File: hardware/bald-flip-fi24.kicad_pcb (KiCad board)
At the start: 4 copper layers, 67.3 x 37.3 mm, 35 parts, among them J1 Flipper Header, J2 USB4105-GF-A, J3 Flipper Board Outline (Large), Q1 DMN2058U, Q2 DMN2058U, SW1 5V Src, SW2 nRF PWR, SW3 Boot, SW4 Reset, SW5 esp PWR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

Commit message: moved nrf24 to front, I like it better
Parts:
- added D5: nRF, LED_SMD:LED_0805_2012Metric_Pad1.15x1.40mm_HandSolder, F.Cu at (141.2, 105.1)
- added R12: 4k7, Resistor_SMD:R_0805_2012Metric, F.Cu at (137.5, 105.1)
- D1: footprint LED_SMD:LED_1206_3216Metric -> LED_SMD:LED_0805_2012Metric_Pad1.15x1.40mm_HandSolder
- D2: value 3v3 -> ESP; footprint LED_SMD:LED_1206_3216Metric -> LED_SMD:LED_0805_2012Metric_Pad1.15x1.40mm_HandSolder
- TP1: moved to B.Cu
- U2: moved to F.Cu
- moved R2 42.9 mm to (176.8, 101.7)
- moved D2 42.1 mm to (180.7, 101.7)
- moved TP1 28.2 mm to (151.0, 104.0), turned to -90 degrees
- moved D1 27.9 mm to (141.0, 94.4)
- moved R1 24.1 mm to (140.9, 96.7)
- moved C5 19.3 mm to (121.3, 99.5), turned to 180 degrees
- moved C4 15.5 mm to (134.2, 99.5), turned to 0 degrees
- moved C1 14.6 mm to (121.3, 104.7), turned to 180 degrees
- moved U2 12.0 mm to (143.9, 119.8)
- moved U3 10.3 mm to (127.6, 102.1), turned to 180 degrees
- moved J3 9.97 mm to (123.5, 109.2)
- moved C2 1.90 mm to (173.1, 101.7)
- moved R4 1.64 mm to (169.4, 101.7)
- moved C3 1.60 mm to (158.2, 101.7)
- moved R3 1.56 mm to (165.7, 101.7)
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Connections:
- R2 pad 1: +3V3 -> /esp_VCC
- R4 pad 1: +3V3 -> /esp_VCC
- R5 pad 1: +3V3 -> /esp_VCC

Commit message: re-worked SPi signals, need to consider if firmware can handle moving CS. Cleaned up some silk (for now).
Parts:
- added NT1: NetTie_2, NetTie:NetTie-2_SMD_Pad0.5mm, F.Cu at (133.4, 124.7)
- added NT2: NetTie_2, NetTie:NetTie-2_SMD_Pad0.5mm, F.Cu at (135.9, 124.6)
- added NT3: NetTie_2, NetTie:NetTie-2_SMD_Pad0.5mm, F.Cu at (123.2, 124.6)
- added NT4: NetTie_2, NetTie:NetTie-2_SMD_Pad0.5mm, F.Cu at (125.8, 124.6)
- added NT5: NetTie_2, NetTie:NetTie-2_SMD_Pad0.5mm, F.Cu at (128.3, 124.6)
- added NT6: NetTie_2, NetTie:NetTie-2_SMD_Pad0.5mm, F.Cu at (130.8, 124.6)
- J3: moved to B.Cu
- SW1: value 5V Src -> 5V
- SW2: value nRF PWR -> nRF
- SW5: value esp PWR -> esp
- moved D3 24.1 mm to (150.2, 121.8), turned to 180 degrees
- moved D4 21.0 mm to (150.1, 116.2), turned to 180 degrees
- moved R1 1.47 mm to (141.0, 98.2)
- moved D1 1.40 mm to (141.0, 95.8)
- moved R7 0.95 mm to (141.0, 100.5), turned to 180 degrees
- moved R10 0.50 mm to (148.8, 123.7)
- turned J3 to 180 degrees
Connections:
- U1 pad 13: unconnected-(U1-GPIO10/ADC1_CH9-Pad13) -> /CS
- U1 pad 14: unconnected-(U1-GPIO11/ADC2_CH0-Pad14) -> /MOSI
- U1 pad 15: unconnected-(U1-GPIO12/ADC2_CH1-Pad15) -> /SCK
- U1 pad 16: unconnected-(U1-GPIO13/ADC2_CH2-Pad16) -> /MISO
- U2 pad 3: /B2 -> /EN_24
- U2 pad 4: /A4 -> /CS
- U2 pad 5: /B3 -> /SCK
- U2 pad 6: /A7 -> /MOSI
- U2 pad 7: /A6 -> /MISO
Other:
- board text added: "When fully assembled, this text is hidden"

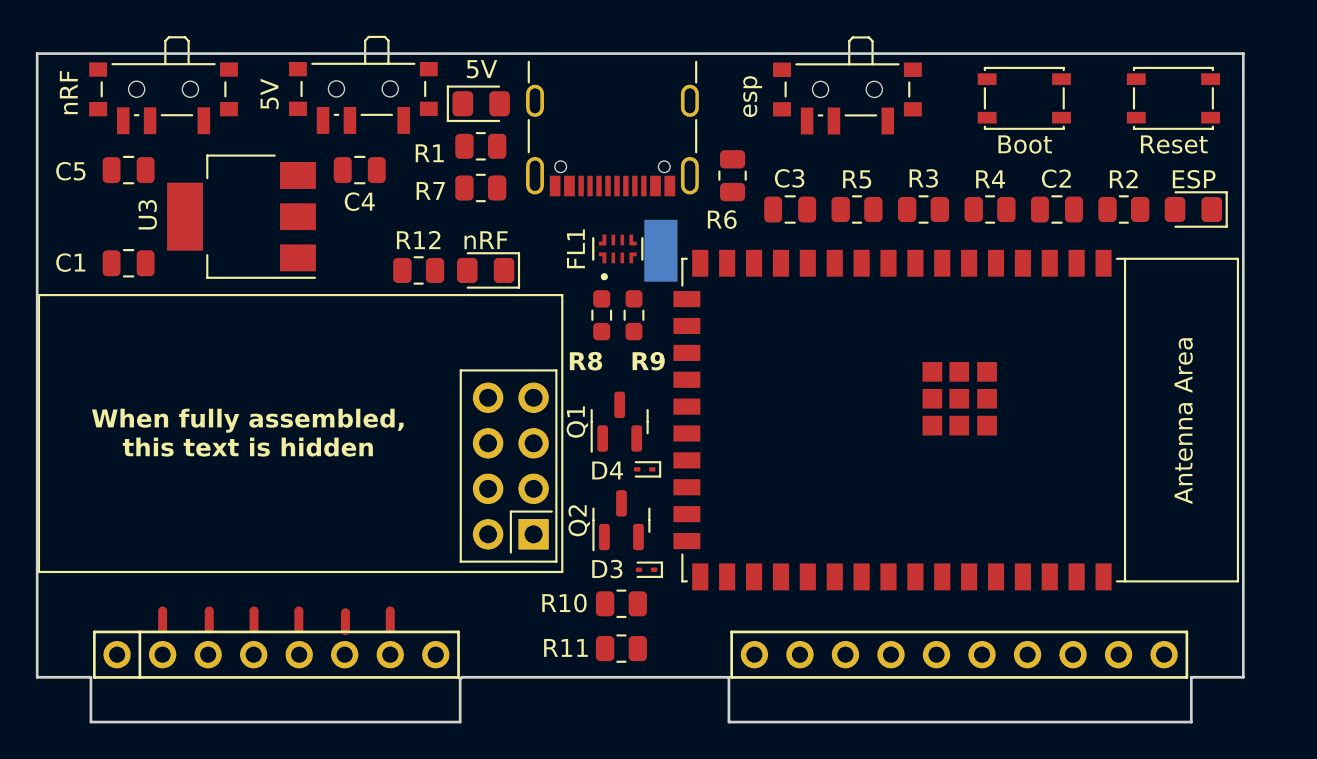
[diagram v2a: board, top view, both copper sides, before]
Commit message: added RGB and test points
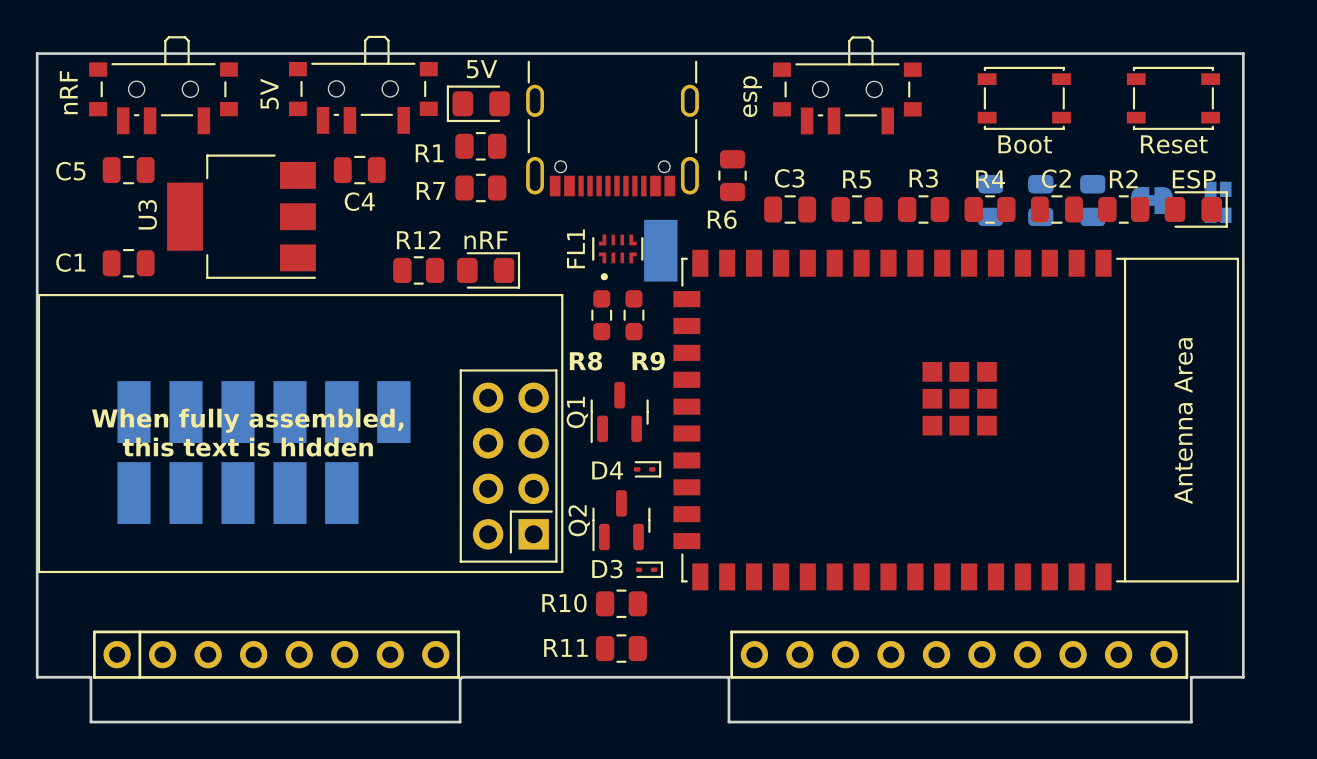
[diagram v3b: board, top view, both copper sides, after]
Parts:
- removed NT1, NT2, NT3, NT4, NT5, NT6: NetTie_2, NetTie:NetTie-2_SMD_Pad0.5mm
- added D6: LTST-C19HE1WT, LED_SMD:LED_LiteOn_LTST-C19HE1WT, B.Cu at (182.1, 101.3)
- added JP1: Jumper_2_Bridged, Jumper:SolderJumper-2_P1.3mm_Bridged_RoundedPad1.0x1.5mm, B.Cu at (178.4, 101.2)
- added R13: 1k, Resistor_SMD:R_0805_2012Metric, B.Cu at (169.4, 101.2)
- added R14: 1k, Resistor_SMD:R_0805_2012Metric, B.Cu at (175.1, 101.2)
- added R15: 5.1k, Resistor_SMD:R_0805_2012Metric, B.Cu at (172.2, 101.2)
- added TP10: TestPoint_Harwin, My Libraries:Harwin-S1751-46-Test-Point, B.Cu at (127.4, 117.5)
- added TP11: TestPoint_Harwin, My Libraries:Harwin-S1751-46-Test-Point, B.Cu at (130.3, 117.5)
- added TP12: TestPoint_Harwin, My Libraries:Harwin-S1751-46-Test-Point, B.Cu at (133.2, 117.5)
- added TP2: TestPoint_Harwin, My Libraries:Harwin-S1751-46-Test-Point, B.Cu at (121.6, 113.0)
- added TP3: TestPoint_Harwin, My Libraries:Harwin-S1751-46-Test-Point, B.Cu at (124.5, 113.0)
- added TP4: TestPoint_Harwin, My Libraries:Harwin-S1751-46-Test-Point, B.Cu at (127.4, 113.0)
- added TP5: TestPoint_Harwin, My Libraries:Harwin-S1751-46-Test-Point, B.Cu at (130.3, 113.0)
- added TP6: TestPoint_Harwin, My Libraries:Harwin-S1751-46-Test-Point, B.Cu at (133.2, 113.0)
- added TP7: TestPoint_Harwin, My Libraries:Harwin-S1751-46-Test-Point, B.Cu at (136.1, 113.0)
- added TP8: TestPoint_Harwin, My Libraries:Harwin-S1751-46-Test-Point, B.Cu at (121.6, 117.5)
- added TP9: TestPoint_Harwin, My Libraries:Harwin-S1751-46-Test-Point, B.Cu at (124.5, 117.5)
- moved Q1 0.54 mm to (148.7, 113.0)
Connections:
- D3 pad 2: /ESP_EN -> /C3
- D4 pad 2: /FLP_GPIO_0 -> /B2
- Q1 pad 2: /FLP_GPIO_0 -> /B2
- Q2 pad 2: /ESP_EN -> /C3
- R10 pad 2: /ESP_EN -> /C3
- R11 pad 2: /FLP_GPIO_0 -> /B2
- SW1 pad 1: /Flip_5V -> /VBUS
- SW1 pad 3: /VBUS -> /Flip_5V
- SW2 pad 1: +3V3 -> unconnected-(SW2-A-Pad1)
- SW2 pad 3: unconnected-(SW2-C-Pad3) -> +3V3
- SW5 pad 1: +3V3 -> unconnected-(SW5-A-Pad1)
- SW5 pad 3: unconnected-(SW5-C-Pad3) -> +3V3
- U1 pad 13: /CS -> /B3
- U1 pad 14: /MOSI -> /A7
- U1 pad 15: /SCK -> /A4
- U1 pad 16: /MISO -> /A6
- U1 pad 6: unconnected-(U1-GPIO3/ADC1_CH2-Pad6) -> /I2C_PU
- U1 pad 7: unconnected-(U1-GPIO4/ADC1_CH3-Pad7) -> /Blu
- U1 pad 8: unconnected-(U1-GPIO5/ADC1_CH4-Pad8) -> /Grn
- U1 pad 9: unconnected-(U1-GPIO6/ADC1_CH5-Pad9) -> /Red
- U2 pad 4: /CS -> /B3
- U2 pad 5: /SCK -> /A4
- U2 pad 6: /MOSI -> /A7
- U2 pad 7: /MISO -> /A6
